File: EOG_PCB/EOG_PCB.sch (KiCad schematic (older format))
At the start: 38 parts, among them J1 Conn_01x03_Female, J2 POWER INPUT, J3 SIGNAL INPUT, J4 OUT, U1 TL082, U2 TL082, U3 TL082, U4 LM7805_TO220, U5 LM7905_TO220, U6 INA114AP

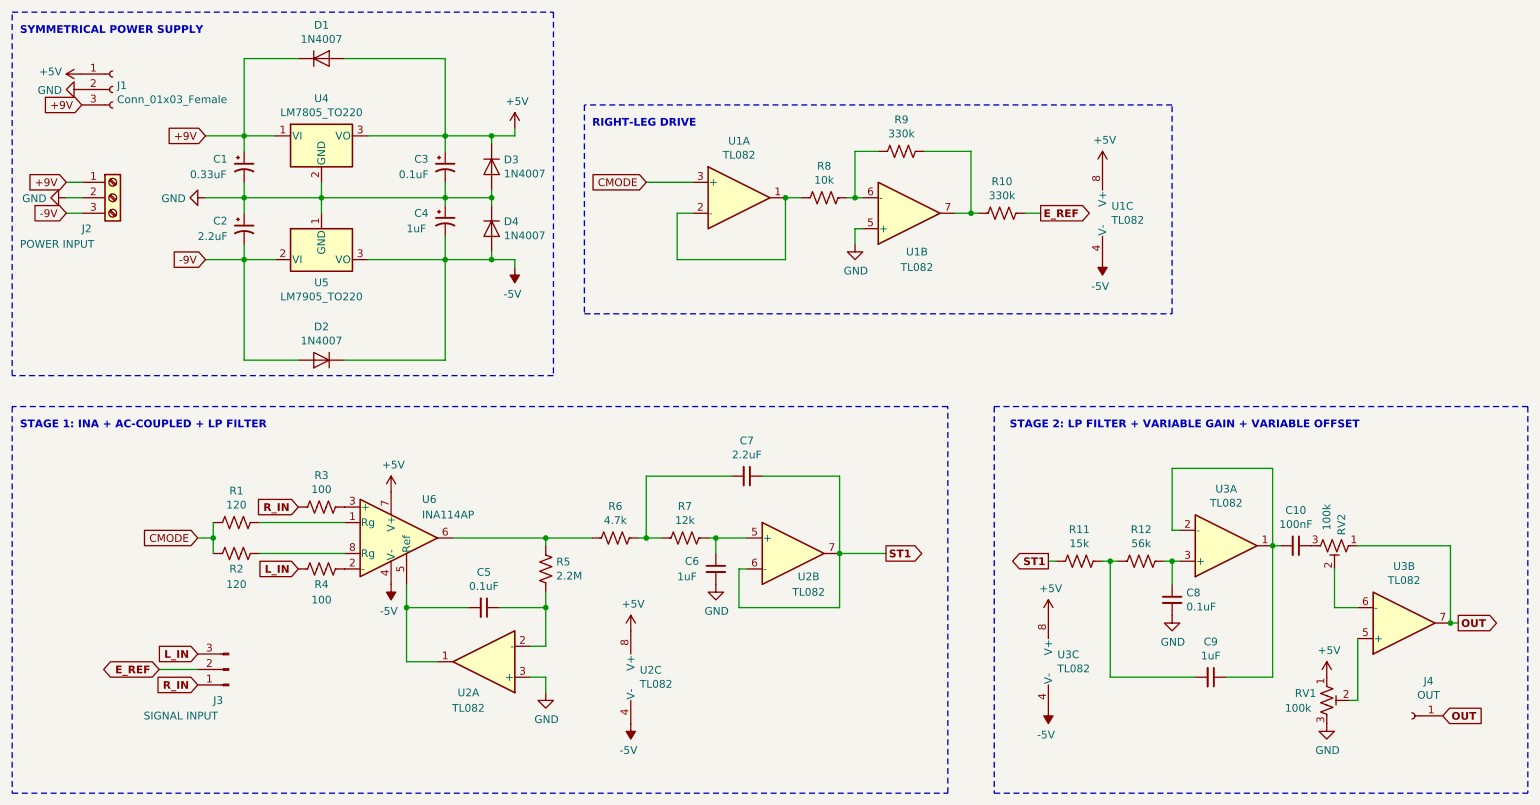
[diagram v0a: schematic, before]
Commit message: Added PCB Layout & Minor Improvements in sch
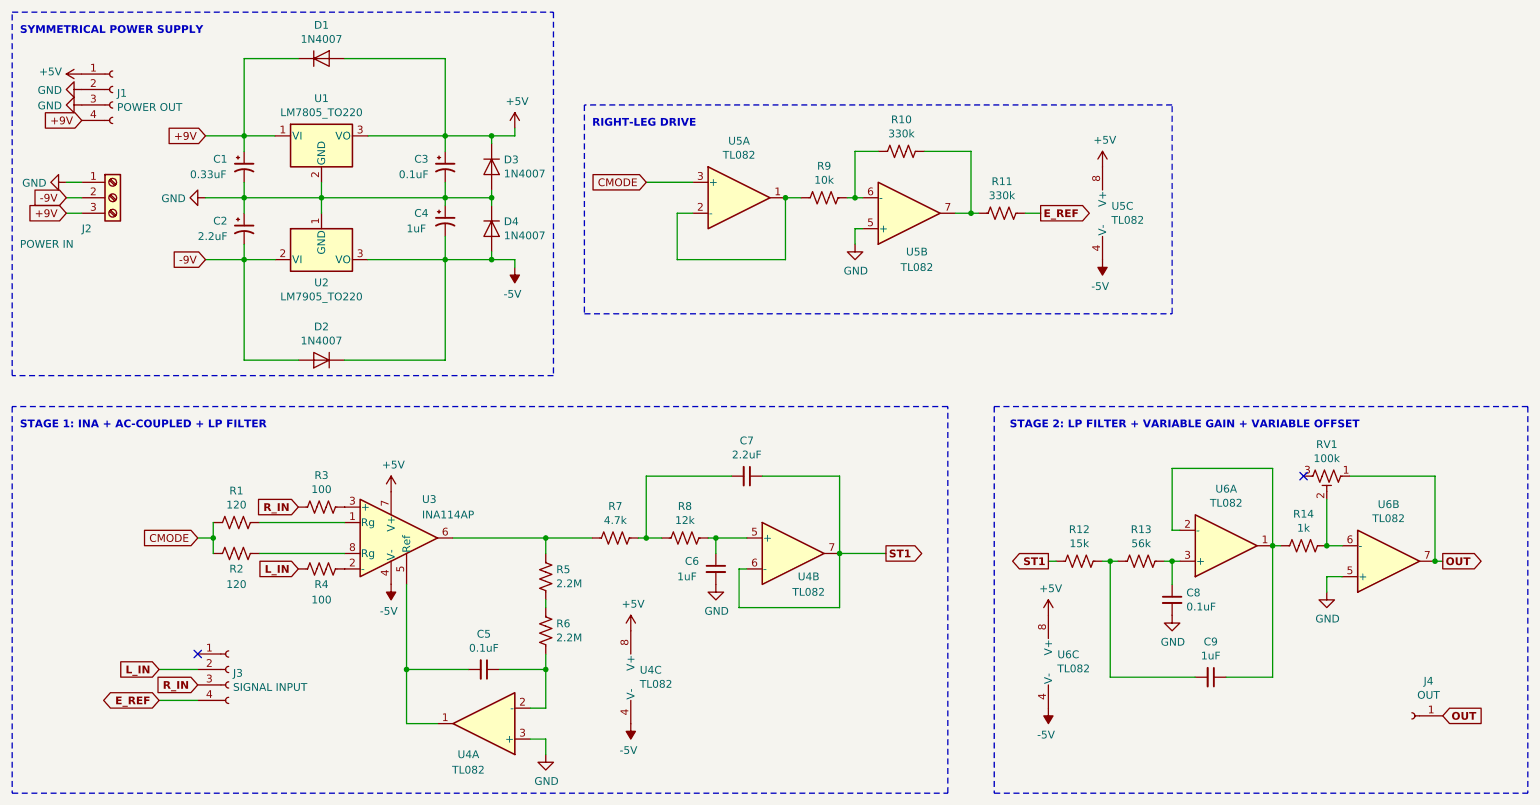
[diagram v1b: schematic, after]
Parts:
- removed C10: 100nF, symbol Device:C_Small
- removed J1: Conn_01x03_Female, symbol Connector:Conn_01x03_Female
- removed J3: SIGNAL INPUT, symbol Connector:Conn_01x03_Male
- removed RV2: 100k, symbol Device:R_POT_TRIM_US
- added J1: POWER OUT, Connector_PinSocket_2.54mm:PinSocket_1x04_P2.54mm_Vertical, symbol Connector:Conn_01x04_Female
- added J3: SIGNAL INPUT, Connector_PinSocket_2.54mm:PinSocket_1x04_P2.54mm_Vertical, symbol Connector:Conn_01x04_Female
- added R14: 1k, Resistor_THT:R_Axial_DIN0204_L3.6mm_D1.6mm_P5.08mm_Horizontal, symbol Device:R_US
- added R5: 2.2M, Resistor_THT:R_Axial_DIN0204_L3.6mm_D1.6mm_P5.08mm_Horizontal, symbol Device:R_US
- C1: footprint (none) -> Capacitor_THT:CP_Radial_Tantal_D4.5mm_P2.50mm
- C2, C4: footprint (none) -> Capacitor_THT:CP_Radial_D6.3mm_P2.50mm
- C3, C5, C8: footprint (none) -> Capacitor_THT:C_Rect_L7.2mm_W2.5mm_P5.00mm_FKS2_FKP2_MKS2_MKP2
- C6, C7, C9: footprint (none) -> Capacitor_THT:C_Rect_L24.0mm_W7.0mm_P22.50mm_MKT
- J2: value POWER INPUT -> POWER IN; footprint (none) -> TerminalBlock_Philmore:TerminalBlock_Philmore_TB133_1x03_P5.00mm_Horizontal
- J4: footprint (none) -> Connector_PinHeader_2.54mm:PinHeader_1x01_P2.54mm_Vertical
- R1, R2, R3, R4: footprint (none) -> Resistor_THT:R_Axial_DIN0204_L3.6mm_D1.6mm_P5.08mm_Horizontal
- R10: renamed from R9; footprint (none) -> Resistor_THT:R_Axial_DIN0204_L3.6mm_D1.6mm_P5.08mm_Horizontal
- R11: renamed from R10; footprint (none) -> Resistor_THT:R_Axial_DIN0204_L3.6mm_D1.6mm_P5.08mm_Horizontal
- R12: renamed from R11; footprint (none) -> Resistor_THT:R_Axial_DIN0204_L3.6mm_D1.6mm_P5.08mm_Horizontal
- R13: renamed from R12; footprint (none) -> Resistor_THT:R_Axial_DIN0204_L3.6mm_D1.6mm_P5.08mm_Horizontal
- R6: renamed from R5; footprint (none) -> Resistor_THT:R_Axial_DIN0204_L3.6mm_D1.6mm_P5.08mm_Horizontal
- R7: renamed from R6; footprint (none) -> Resistor_THT:R_Axial_DIN0204_L3.6mm_D1.6mm_P5.08mm_Horizontal
- R8: renamed from R7; footprint (none) -> Resistor_THT:R_Axial_DIN0204_L3.6mm_D1.6mm_P5.08mm_Horizontal
- R9: renamed from R8; footprint (none) -> Resistor_THT:R_Axial_DIN0204_L3.6mm_D1.6mm_P5.08mm_Horizontal
- RV1: footprint (none) -> Potentiometer_THT:Potentiometer_Bourns_3386F_Vertical
- U3: renamed from U6; footprint (none) -> Package_DIP:DIP-8_W7.62mm_Socket_LongPads
- U4: renamed from U2; footprint (none) -> Package_DIP:DIP-8_W7.62mm_Socket_LongPads
- U5: renamed from U1; footprint (none) -> Package_DIP:DIP-8_W7.62mm_Socket_LongPads
- U6: renamed from U3; footprint (none) -> Package_DIP:DIP-8_W7.62mm_Socket_LongPads
- renumbered U4 to U1, U5 to U2
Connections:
- net +5V: now also J1.1 (Pin_1); no longer RV1.1
- net +9V: now also J2.3 (Pin_3), J1.4 (Pin_4); no longer J2.1 (Pin_1)
- net -9V: now also J2.2 (Pin_2); no longer J2.3 (Pin_3)
- net E_REF: now also J3.4 (Pin_4)
- net GND: now also J2.1 (Pin_1), U6.5 (+), J1.2 (Pin_2), J1.3 (Pin_3); no longer J2.2 (Pin_2), RV1.3
- net L_IN: now also J3.2 (Pin_2)
- net OUT: now also RV1.1
- net R_IN: now also J3.3 (Pin_3)
- net at R7.2, U3.6: now also R5.2; no longer R6.2
- net at C9.1, U6.1, U6.2 (-): now also R14.2
- net at RV1.2: now also U6.6 (-), R14.1; no longer U6.5 (+)
- new net: R5.1, R6.2
- no-connect marks 0 -> 2
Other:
- moved on the sheet: C5, R6, U4A, U6B
